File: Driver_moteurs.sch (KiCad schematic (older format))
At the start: 17 parts, among them Q5 BSS138, Q6 BSS138, Q7 BSS138, U4 LM317_TO3, U5 L293D, U6 L293D

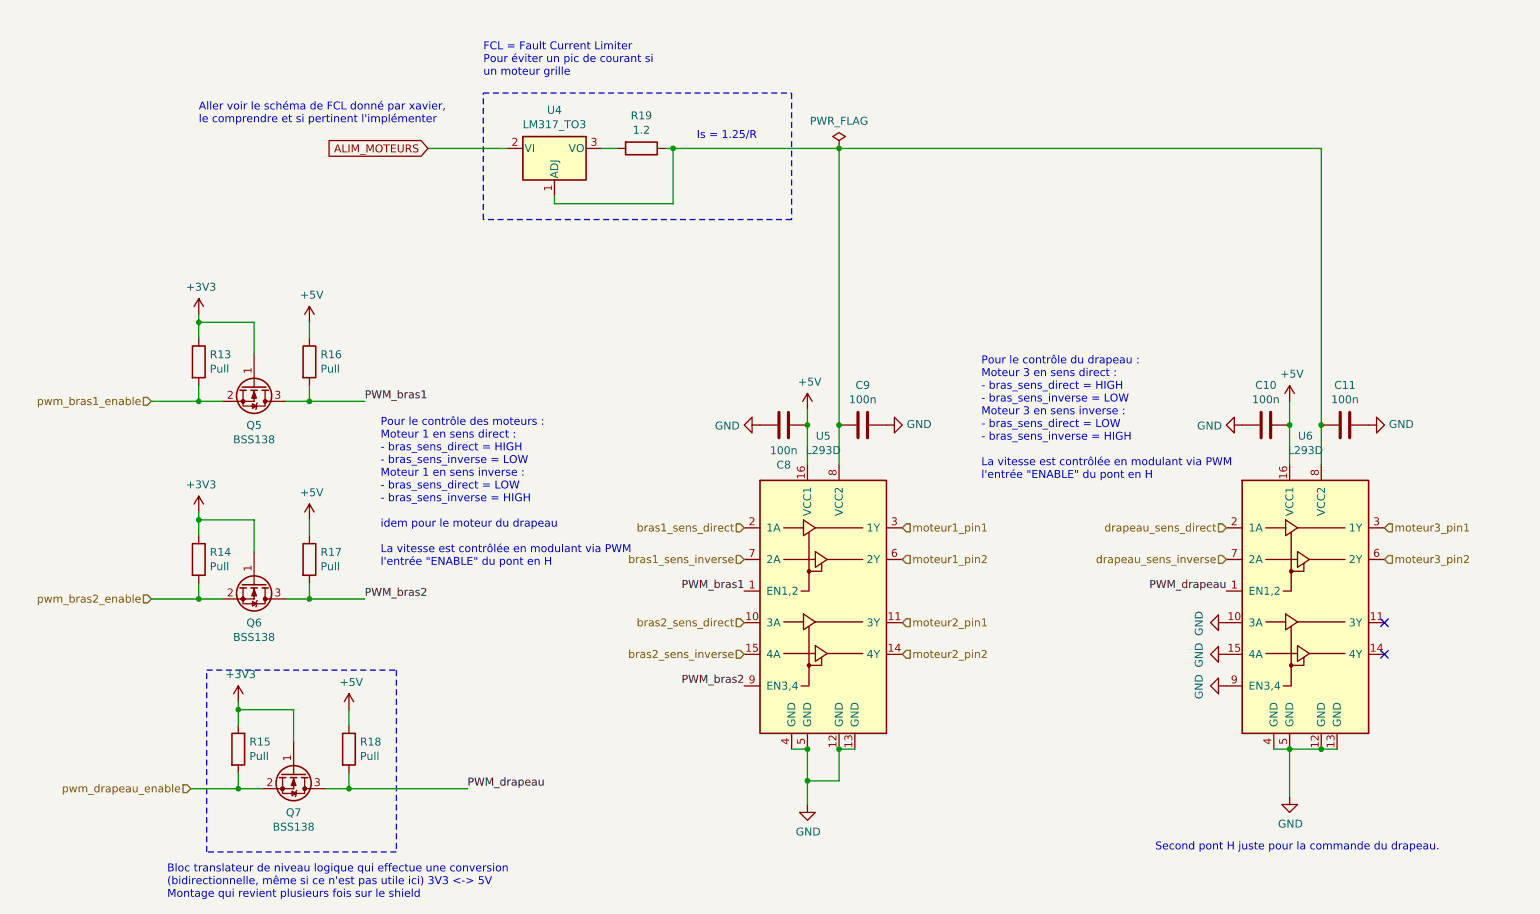
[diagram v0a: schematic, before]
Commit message: removed psi-things pins, added transceiver MCP2551 for CAN, changed motors input protocol, RS must be chosen 1 or 10 kohms, and a foot print for a potentitial 120 ohms resistor is present for CAN bus end.
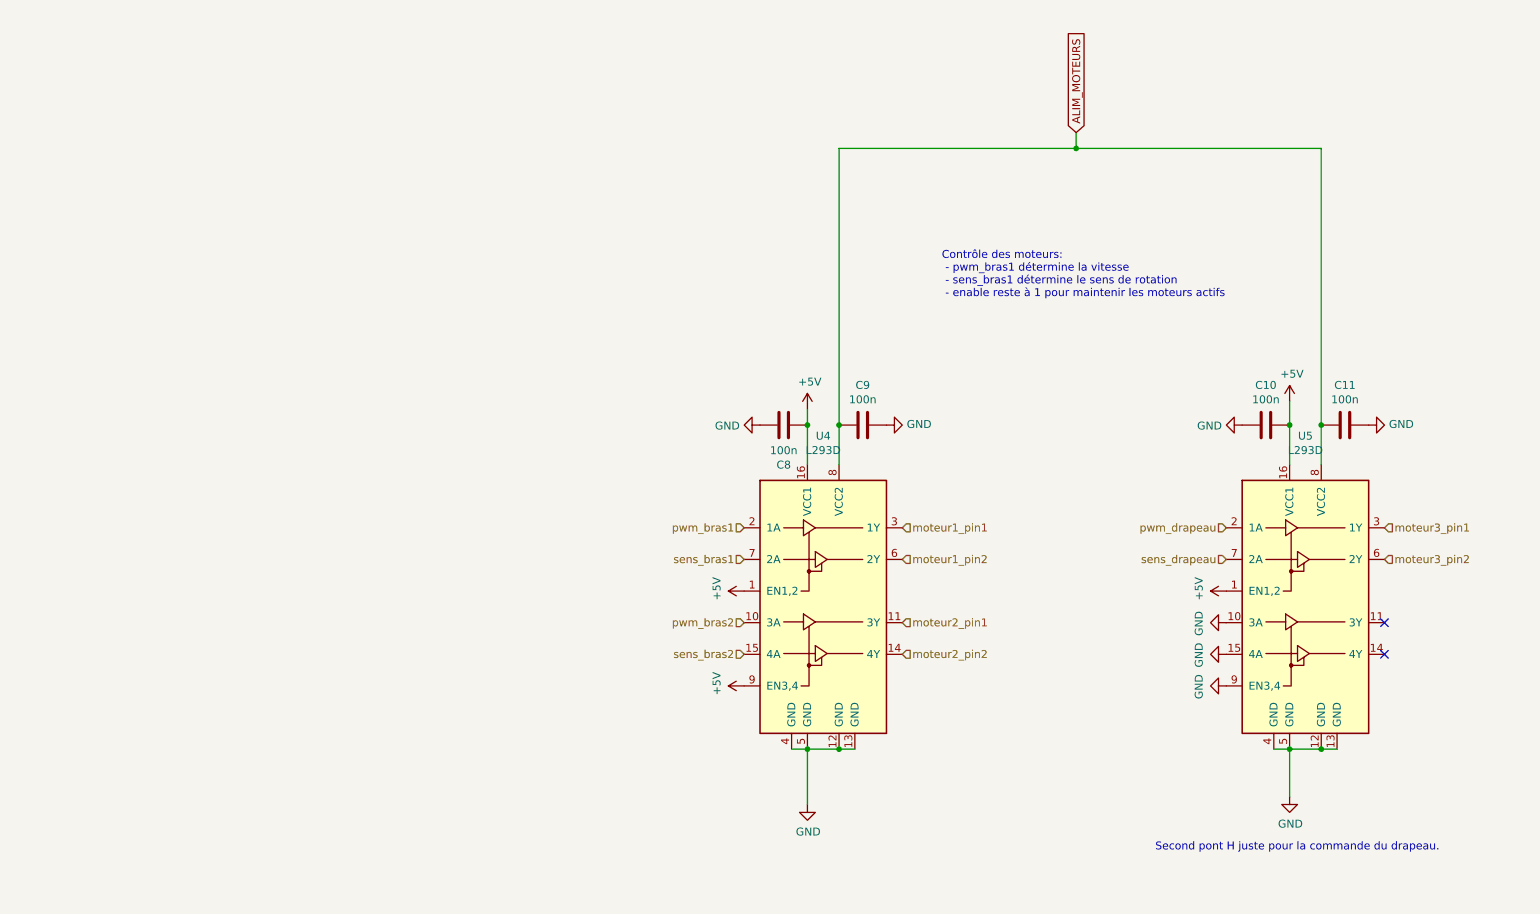
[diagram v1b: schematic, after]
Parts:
- removed Q5, Q6, Q7: BSS138, Package_TO_SOT_SMD:SOT-23, symbol shield_etage2-rescue:BSS138-Transistor_FET-shield_etage2-rescue
- removed R13, R14, R15, R16, R17, R18: Pull, Resistor_SMD:R_0805_2012Metric_Pad1.15x1.40mm_HandSolder, symbol shield_etage2-rescue:R-Device-shield_etage2-rescue
- removed R19: 1.2, Resistor_THT:R_Axial_DIN0414_L11.9mm_D4.5mm_P15.24mm_Horizontal, symbol shield_etage2-rescue:R-Device-shield_etage2-rescue
- removed U4: LM317_TO3, Package_TO_SOT_THT:TO-220-3_Vertical, symbol shield_etage2-rescue:LM317_TO3-Regulator_Linear-shield_etage2-rescue
- renumbered U5 to U4, U6 to U5
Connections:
- net PWM_bras1 is gone; now on net +5V: U4.1 (EN1,2)
- net PWM_bras2 is gone; now on net +5V: U4.9 (EN3,4)
- net PWM_drapeau is gone; now on net +5V: U5.1 (EN1,2)
- net ALIM_MOTEURS: now also C11.2, C9.2, U4.8 (VCC2), U5.8 (VCC2)
- net bras1_sens_direct renamed pwm_bras1
- net bras1_sens_inverse renamed sens_bras1
- net bras2_sens_direct renamed pwm_bras2
- net bras2_sens_inverse renamed sens_bras2
- net drapeau_sens_direct renamed pwm_drapeau
- net drapeau_sens_inverse renamed sens_drapeau
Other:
- note added: "Contrôle des moteurs:\n - pwm_bras1 détermine la vitesse\n - sens_bras1 détermine le sens de rotation\n - enable reste à 1 pour maintenir les moteurs actifs"
- note removed: "Aller voir le schéma de FCL donné par xavier, \nle comprendre et si pertinent l'implémenter"
- note removed: "Bloc translateur de niveau logique qui effectue une conversion \n(bidirectionnelle, même si ce n'est pas utile ici) 3V3 <-> 5V\nMontage qui revient plusieurs fois sur le shield"
- note removed: "FCL = Fault Current Limiter\nPour éviter un pic de courant si\nun moteur grille"
- note removed: "Is = 1.25/R\n"
- note removed: "Pour le contrôle des moteurs :\nMoteur 1 en sens direct : \n- bras_sens_direct = HIGH\n- bras_sens_inverse = LOW\nMoteur 1 en sens inverse : \n- bras_sens_direct = LOW\n- bras_sens_inverse = HIGH\n\nidem pour le moteur du drapeau\n\nLa vitesse est contrôlée en modulant via PWM \nl'entrée "ENABLE" du pont en H"
- note removed: "Pour le contrôle du drapeau :\nMoteur 3 en sens direct : \n- bras_sens_direct = HIGH\n- bras_sens_inverse = LOW\nMoteur 3 en sens inverse : \n- bras_sens_direct = LOW\n- bras_sens_inverse = HIGH\n\nLa vitesse est contrôlée en modulant via PWM \nl'entrée "ENABLE" du pont en H"
